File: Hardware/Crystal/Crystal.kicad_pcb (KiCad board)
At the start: 2 copper layers, 66 x 43 mm, 52 parts, among them J1 USB_B_Micro, U1 AP63205WU, U2 NCP1117-3.3_SOT223, U3 ESP32-C3-WROOM-02, U4 TXS0102DCT, U5 TXS0108EPW

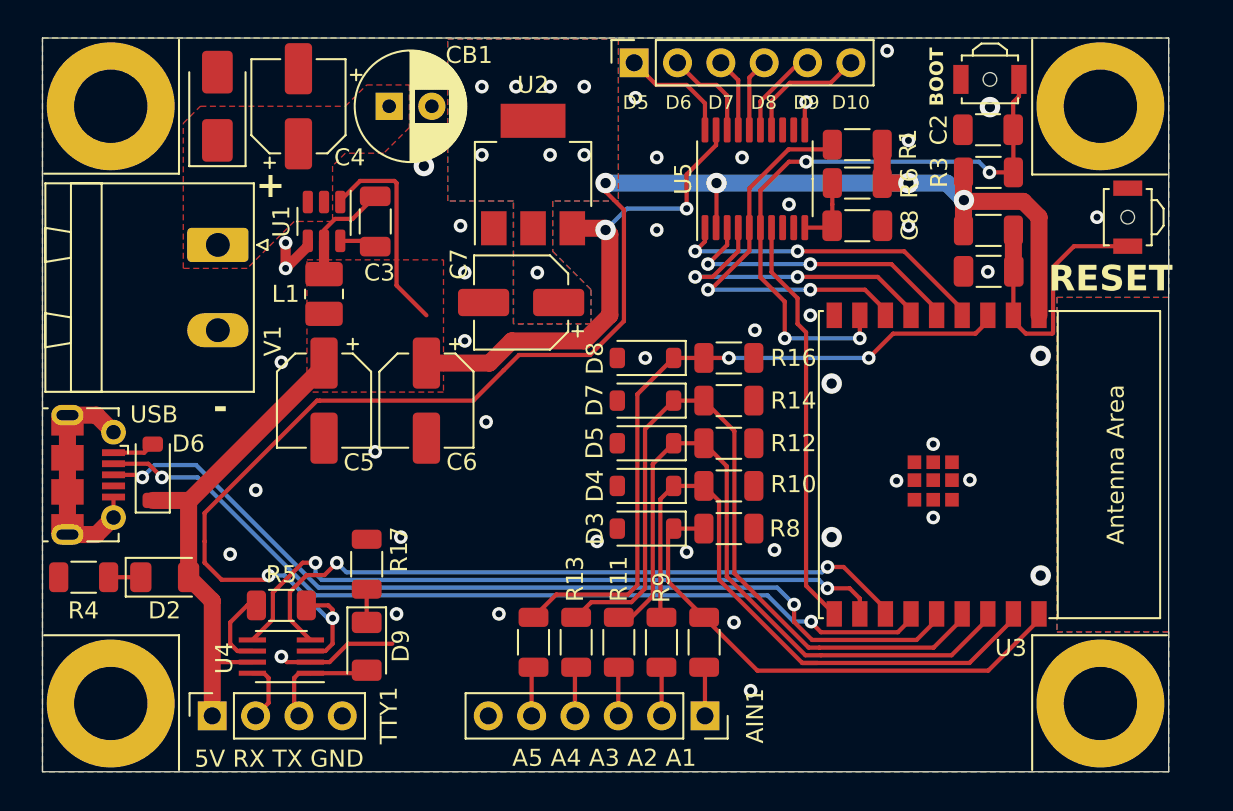
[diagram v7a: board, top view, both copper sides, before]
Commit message: Further PCB revision to use MLCC caps in the 5v regulator for better smoothing and space utilization
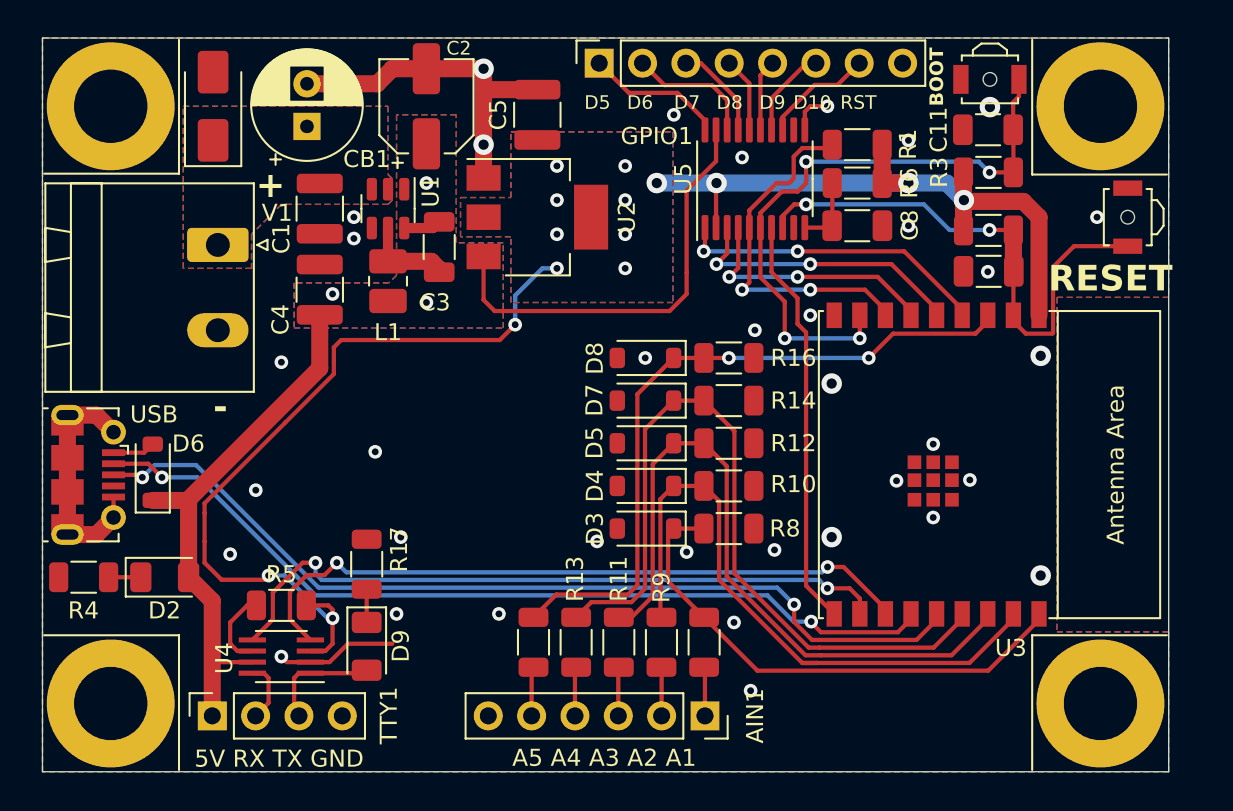
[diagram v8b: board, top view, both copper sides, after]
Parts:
- C1: renamed from C4; value 22uF -> 10uF; footprint Capacitor_SMD:CP_Elec_5x5.3 -> Capacitor_SMD:C_1210_3225Metric
- C4: renamed from C6; value 22uF -> 10uF; footprint Capacitor_SMD:CP_Elec_5x5.3 -> Capacitor_SMD:C_1210_3225Metric
- C5: renamed from C7; value 22uF -> 10uF; footprint Capacitor_SMD:CP_Elec_5x5.3 -> Capacitor_SMD:C_1210_3225Metric
- GPIO1: value Conn_01x06 -> Conn_01x08; footprint Connector_PinSocket_2.54mm:PinSocket_1x06_P2.54mm_Vertical -> Connector_PinSocket_2.54mm:PinSocket_1x08_P2.54mm_Vertical
- moved C2 18.3 mm to (42.5, 24.0), turned to 90 degrees
- moved C5 11.0 mm to (49.0, 24.5), turned to 90 degrees
- moved C4 9.02 mm to (36.2, 34.8), turned to 90 degrees
- moved C1 6.13 mm to (36.2, 30.0), turned to -90 degrees
- moved CB1 4.96 mm to (35.5, 25.2), turned to 90 degrees
- moved C3 4.04 mm to (43.2, 32.2), turned to -90 degrees
- moved L1 3.82 mm to (40.2, 34.2)
- moved U1 3.82 mm to (40.2, 30.0)
- moved U2 2.51 mm to (49.0, 30.5), turned to 0 degrees
- moved GPIO1 2.05 mm to (52.6, 21.5)
- moved D1 0.25 mm to (30.0, 24.0)
- renumbered C1 to C10, C2 to C11, C5 to C2
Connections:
- C10 pad 2: Net-(U3-EN/CHIP_PU) -> /RESET
- R2 pad 2: Net-(U3-EN/CHIP_PU) -> /RESET
- RESET1 pad 2: Net-(U3-EN/CHIP_PU) -> /RESET
- U3 pad 2: Net-(U3-EN/CHIP_PU) -> /RESET
- U5 pad 13: unconnected-(U5-B7-Pad13) -> Net-(GPIO1-Pin_7)
- U5 pad 8: unconnected-(U5-A7-Pad8) -> /RESET
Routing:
- net /RESET: track 0.00 -> 31.8 mm, vias 0 -> 2
- net GND: track 26.8 -> 44.3 mm, vias 43 -> 36
- net Net-(U3-EN/CHIP_PU): track 16.7 -> 0.00 mm
- net +5V: track 71.9 -> 56.7 mm, vias 2 -> 3
- net +3.3V: track 96.7 -> 84.7 mm, vias 14 -> 15
- net Net-(GPIO1-Pin_7): track 0.00 -> 6.56 mm
- net /GPIO7: track 18.3 -> 14.9 mm
- net /GPIO8: track 24.2 -> 21.6 mm
- net Net-(GPIO1-Pin_6): track 7.27 -> 5.31 mm
- net Net-(GPIO1-Pin_2): track 5.72 -> 7.60 mm
- net Net-(GPIO1-Pin_1): track 6.70 -> 8.15 mm
- net Net-(GPIO1-Pin_3): track 4.36 -> 5.70 mm
- net Net-(GPIO1-Pin_5): track 5.37 -> 4.21 mm
- net /GPIO6: track 17.5 -> 16.7 mm
- net /GPIO5: track 19.0 -> 18.3 mm
- added copper zone on B.Cu, net +12V
- added copper zone on B.Cu, net +5V
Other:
- board text added: "RST"
